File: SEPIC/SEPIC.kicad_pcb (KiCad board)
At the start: 2 copper layers, 41.5 x 58.5 mm, 11 parts, among them J1 Barrel Jack, J2 Pin Header, J3 Screw Terminal, Q1 IRF520N, U1 HCPL-3120

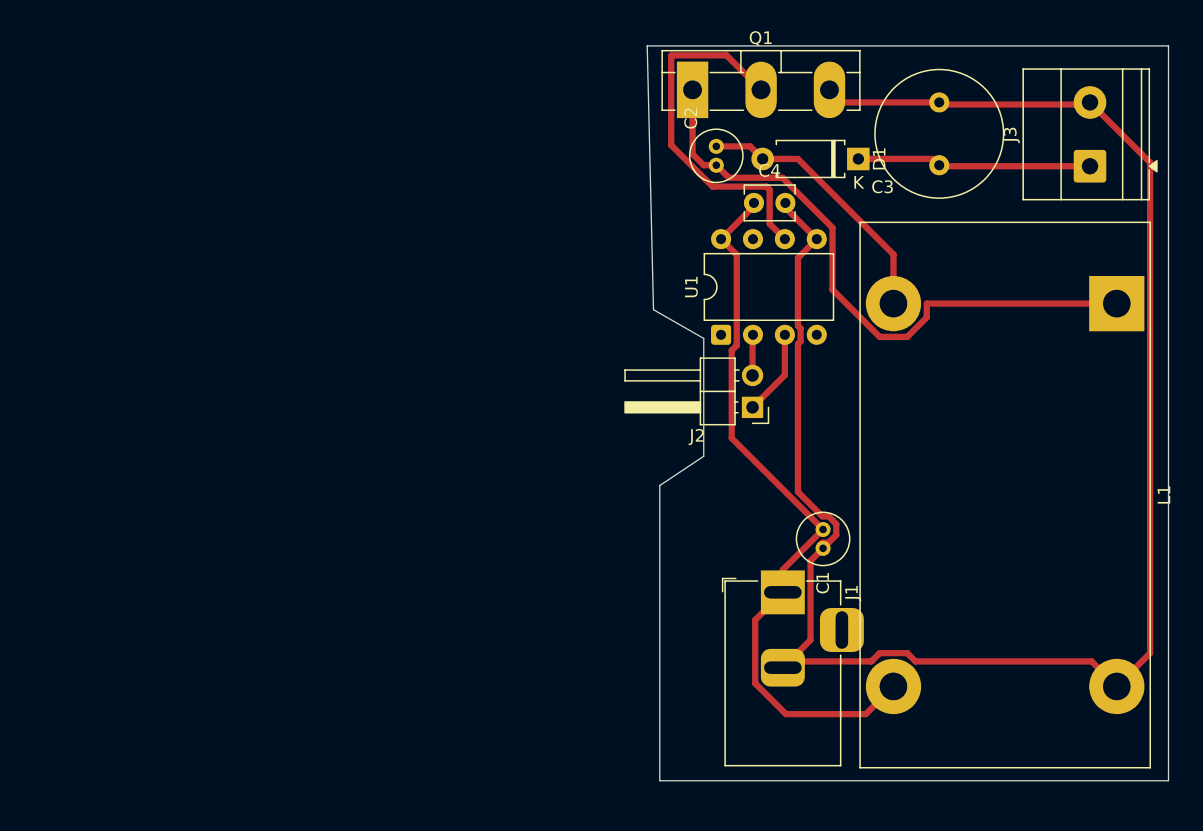
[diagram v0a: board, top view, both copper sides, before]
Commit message: Diseño de PCB finalizado, generación de gerber
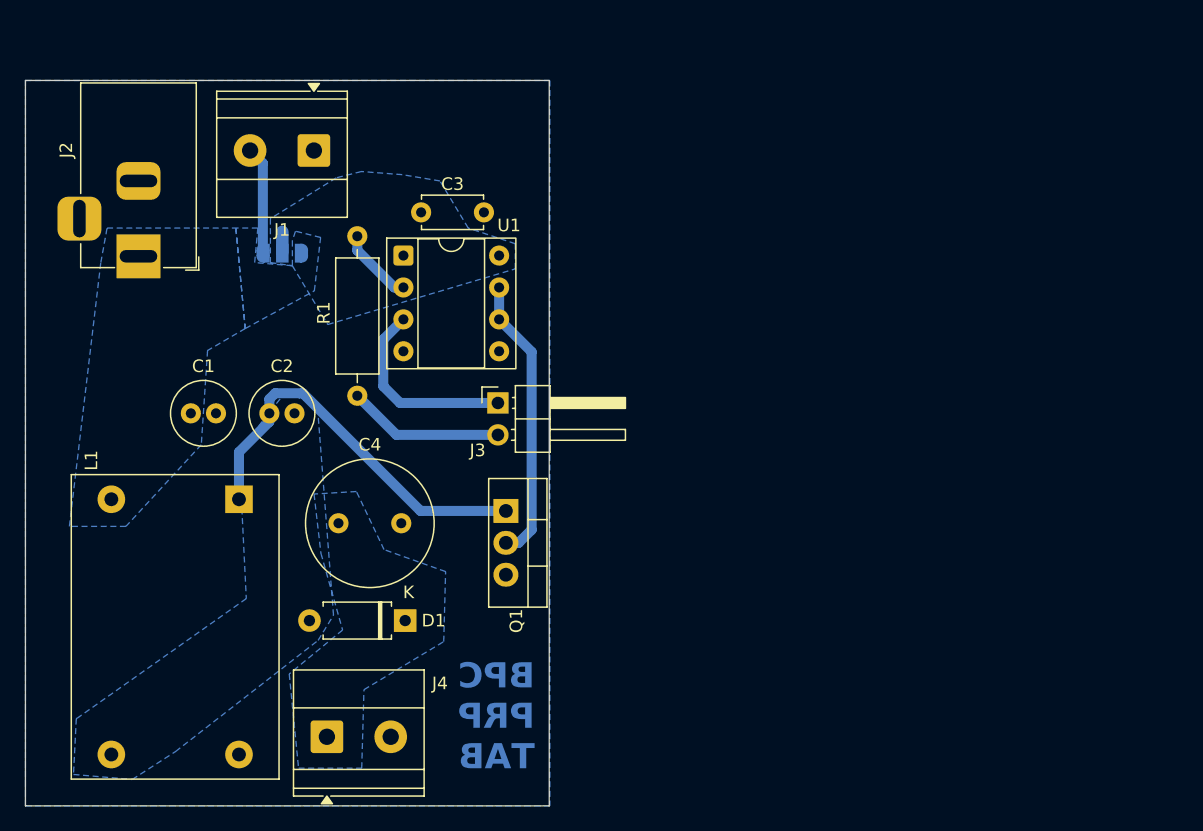
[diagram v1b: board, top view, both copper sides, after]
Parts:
- added J4: Screw Terminal, TerminalBlock_Phoenix:TerminalBlock_Phoenix_MKDS-1,5-2-5.08_1x02_P5.08mm_Horizontal, F.Cu at (65.5, 78.5)
- added JP1: Solder Jumper, Jumper:SolderJumper-3_P1.3mm_Open_RoundedPad1.0x1.5mm, B.Cu at (62.2, 40.0)
- added R1: 220, Resistor_THT:R_Axial_DIN0309_L9.0mm_D3.2mm_P12.70mm_Horizontal, F.Cu at (67.9, 38.6)
- C1, C2: footprint Capacitor_THT:C_Radial_D4.0mm_H7.0mm_P1.50mm -> Capacitor_THT:C_Radial_D5.0mm_H11.0mm_P2.00mm
- C3: value 220u -> 0.1u; footprint Capacitor_THT:C_Radial_D10.0mm_H16.0mm_P5.00mm -> Capacitor_THT:C_Disc_D4.7mm_W2.5mm_P5.00mm
- C4: value 0.1u -> 220u; footprint Capacitor_THT:C_Disc_D3.8mm_W2.6mm_P2.50mm -> Capacitor_THT:C_Radial_D10.0mm_H12.5mm_P5.00mm
- J1: value Barrel Jack -> Screw Terminal; footprint Connector_BarrelJack:BarrelJack_Horizontal -> TerminalBlock_Phoenix:TerminalBlock_Phoenix_MKDS-1,5-2-5.08_1x02_P5.08mm_Horizontal
- J2: value Pin Header -> Barrel Jack; footprint Connector_PinHeader_2.54mm:PinHeader_1x02_P2.54mm_Horizontal -> Connector_BarrelJack:BarrelJack_Horizontal
- J3: value Screw Terminal -> Pin Header; footprint TerminalBlock_Phoenix:TerminalBlock_Phoenix_MKDS-1,5-2-5.08_1x02_P5.08mm_Horizontal -> Connector_PinHeader_2.54mm:PinHeader_1x02_P2.54mm_Horizontal
- L1: footprint Inductor_THT:L_CommonMode_Toroid_Vertical_L43.2mm_W22.9mm_Px17.78mm_Py30.48mm_Bourns_8100 -> Inductor_THT:L_CommonMode_Toroid_Vertical_L24.0mm_W16.3mm_Px10.16mm_Py20.32mm_Murata_5200
- Q1: footprint Package_TO_SOT_THT:TO-3P-3_Vertical -> Package_TO_SOT_THT:TO-220-3_Vertical
- U1: footprint Package_DIP:DIP-8_W7.62mm -> Package_DIP:DIP-8_W7.62mm_Socket
- moved L1 71.6 mm to (58.5, 59.6)
- moved D1 51.5 mm to (71.7, 69.2)
- moved J1 51.3 mm to (64.5, 31.8), turned to 180 degrees
- moved C1 51.2 mm to (54.7, 52.8), turned to 0 degrees
- moved J3 50.8 mm to (79.1, 51.9), turned to 0 degrees
- moved J2 50.3 mm to (50.5, 40.2), turned to -90 degrees
- moved C4 41.8 mm to (66.4, 61.5)
- moved C3 41.4 mm to (73.0, 36.8), turned to 0 degrees
- moved C2 40.7 mm to (60.9, 52.8), turned to 0 degrees
- moved Q1 36.7 mm to (79.8, 60.5), turned to -90 degrees
- moved U1 26.1 mm to (71.6, 40.2), turned to 0 degrees
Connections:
- C3 pad 1: out -> VCC
- C4 pad 1: +24V -> out
- J1 pad 1: +24V -> GND
- J1 pad 2: GND -> Net-(J1-Pin_2)
- J2 pad 1: Net-(J2-Pin_1) -> +24V
- J2 pad 2: Net-(J2-Pin_2) -> GND
- J3 pad 1: out -> Net-(J3-Pin_1)
- J3 pad 2: GND -> Net-(J3-Pin_2)
- L1 pad 2: Net-(D1-A) -> +24V
- L1 pad 3: +24V -> Net-(D1-A)
- U1 pad 2: Net-(J2-Pin_2) -> Net-(U1-A)
- U1 pad 3: Net-(J2-Pin_1) -> Net-(J3-Pin_1)
- U1 pad 7: unconnected-(U1-VO-Pad7) -> PWM
- U1 pad 8: +24V -> VCC
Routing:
- net GND: track 141.4 -> 0.00 mm
- net +24V: track 58.2 -> 0.00 mm
- net Net-(D1-A): track 21.6 -> 0.00 mm
- net out: track 19.2 -> 0.00 mm
- net Net-(Q1-D): track 49.5 -> 31.9 mm
- net Net-(J3-Pin_1): track 0.00 -> 15.7 mm
- net Net-(J3-Pin_2): track 0.00 -> 12.5 mm
- net Net-(J1-Pin_2): track 0.00 -> 8.59 mm
- net Net-(J2-Pin_1): track 6.84 -> 0.00 mm
- net PWM: track 29.2 -> 22.8 mm
- net Net-(U1-A): track 0.00 -> 6.02 mm
- net Net-(J2-Pin_2): track 3.25 -> 0.00 mm
- net VCC: track 0.00 -> 1.77 mm
- added copper zone on B.Cu, net +24V
- added copper zone on B.Cu, net GND
- added copper zone on B.Cu, net Net-(D1-A)
- added copper zone on B.Cu, net VCC
- added copper zone on B.Cu, net out
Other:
- board size 41.5 x 58.5 mm -> 41.7 x 57.8 mm
- board text added: "BPC PRP TAB"

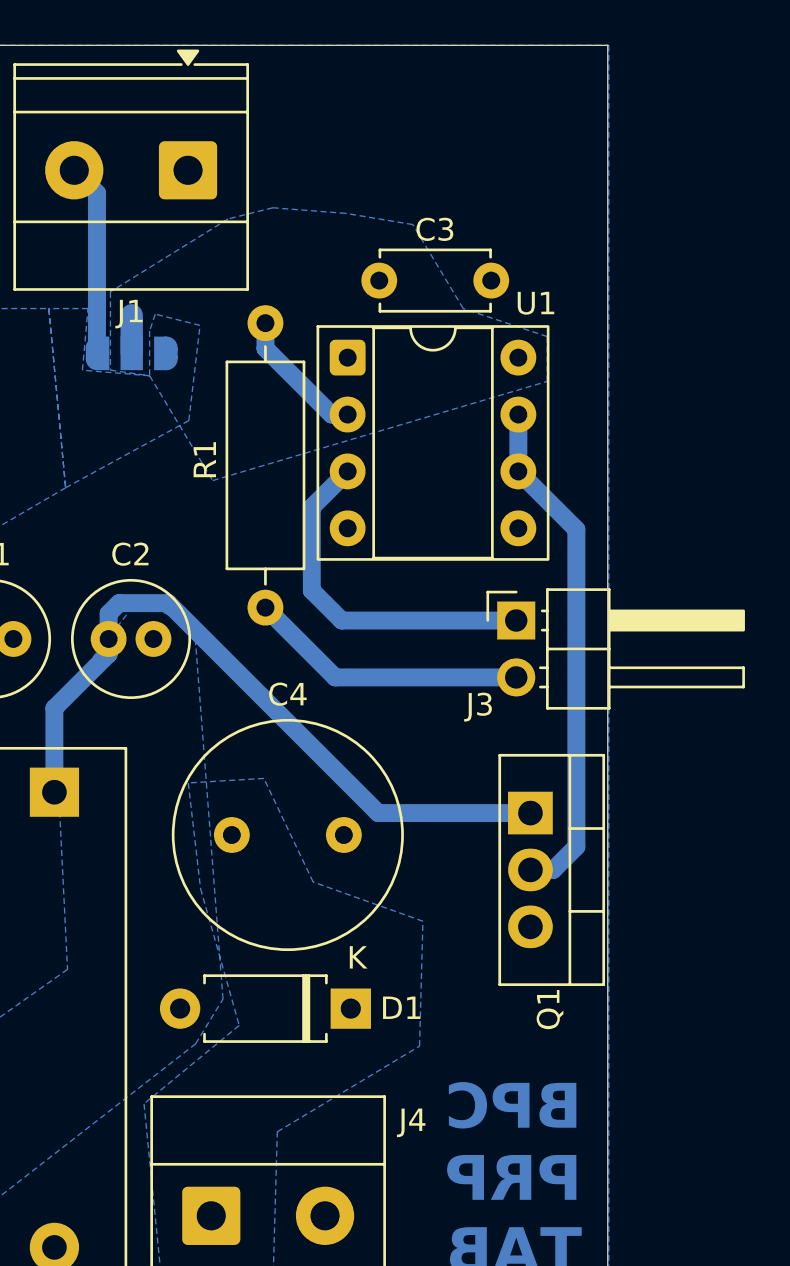
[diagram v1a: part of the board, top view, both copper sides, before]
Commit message: Arreglar pines MOSFET
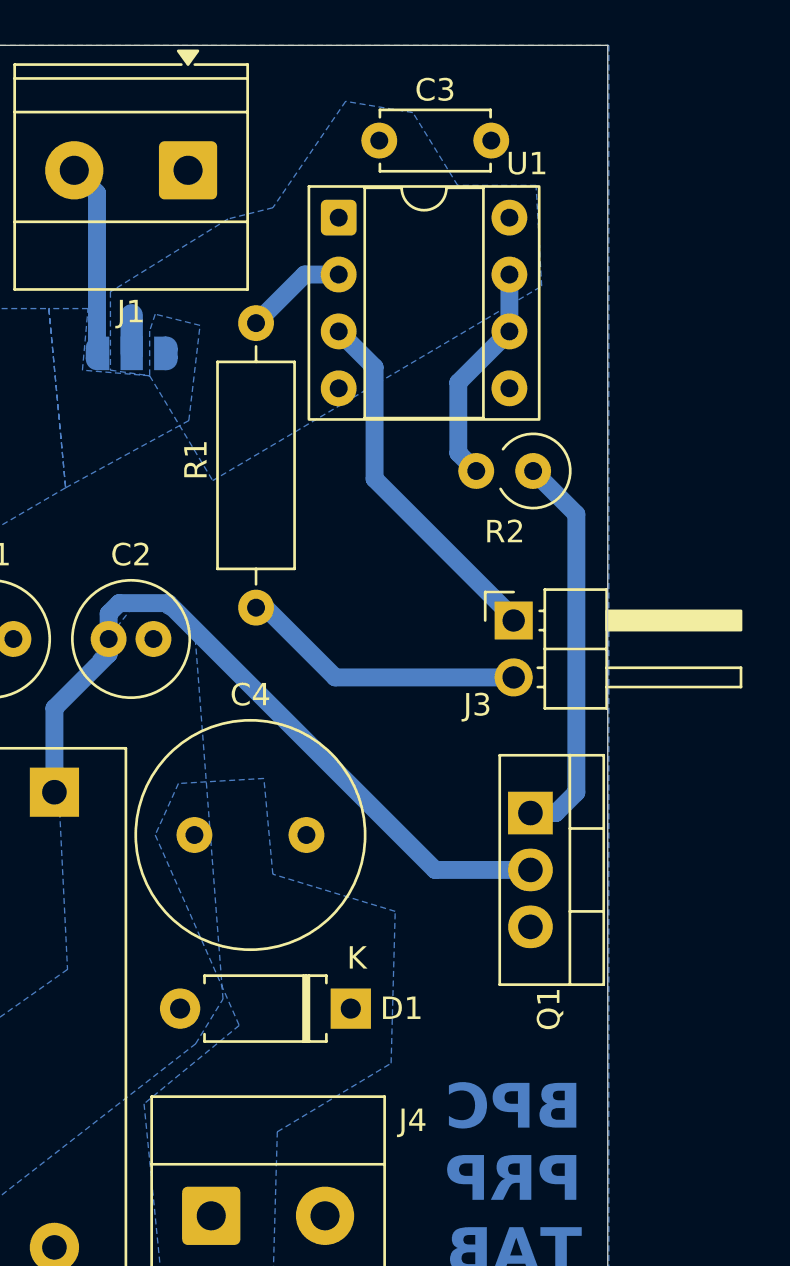
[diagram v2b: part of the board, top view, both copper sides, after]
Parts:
- added R2: 0, Resistor_THT:R_Axial_DIN0309_L9.0mm_D3.2mm_P2.54mm_Vertical, F.Cu at (79.9, 45.2)
- moved U1 6.26 mm to (71.2, 33.9)
- moved C3 6.25 mm to (73.0, 30.5)
- moved C4 1.67 mm to (64.8, 61.5)
- moved R1 0.42 mm to (67.5, 38.6)
- moved J3 0.11 mm to (79.0, 51.9)
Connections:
- Q1 pad 1: Net-(Q1-D) -> PWM
- Q1 pad 2: PWM -> Net-(Q1-D)
- U1 pad 6: PWM -> Net-(R2-Pad2)
- U1 pad 7: PWM -> Net-(R2-Pad2)
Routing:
- net Net-(R2-Pad2): track 0.00 -> 10.0 mm
- net PWM: track 22.8 -> 17.6 mm
- net Net-(U1-A): track 6.02 -> 4.59 mm
- net Net-(Q1-D): track 31.9 -> 32.9 mm
- net Net-(J3-Pin_1): track 15.7 -> 16.2 mm
